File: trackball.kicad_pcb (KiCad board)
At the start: 2 copper layers, 27.5 x 35.2 mm, 37 parts, among them P1 CONN_10, P2 CONN_5, U1 MKL03Z32VFK4, U2 ADNS-3530, U4 ESD

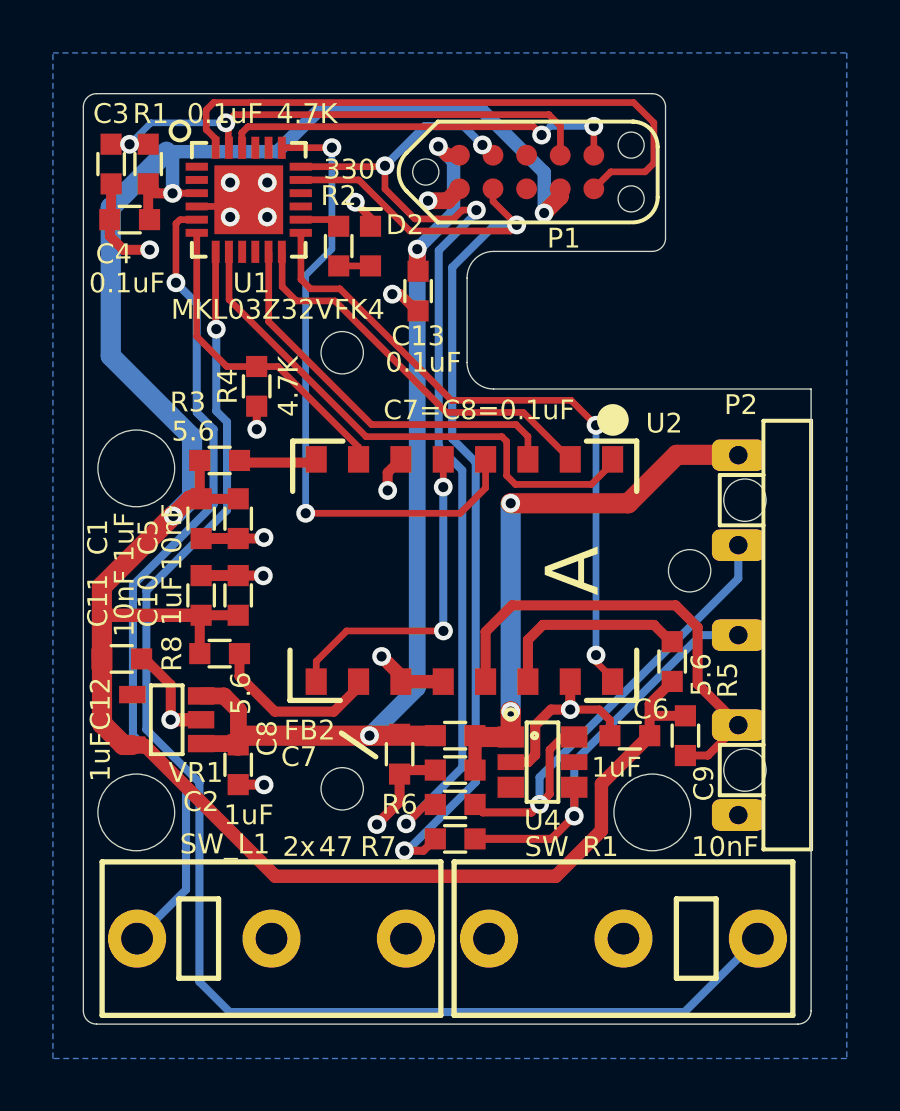
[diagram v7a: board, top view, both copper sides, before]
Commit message: Display optical sensor and microswitch part number on the silk screen.
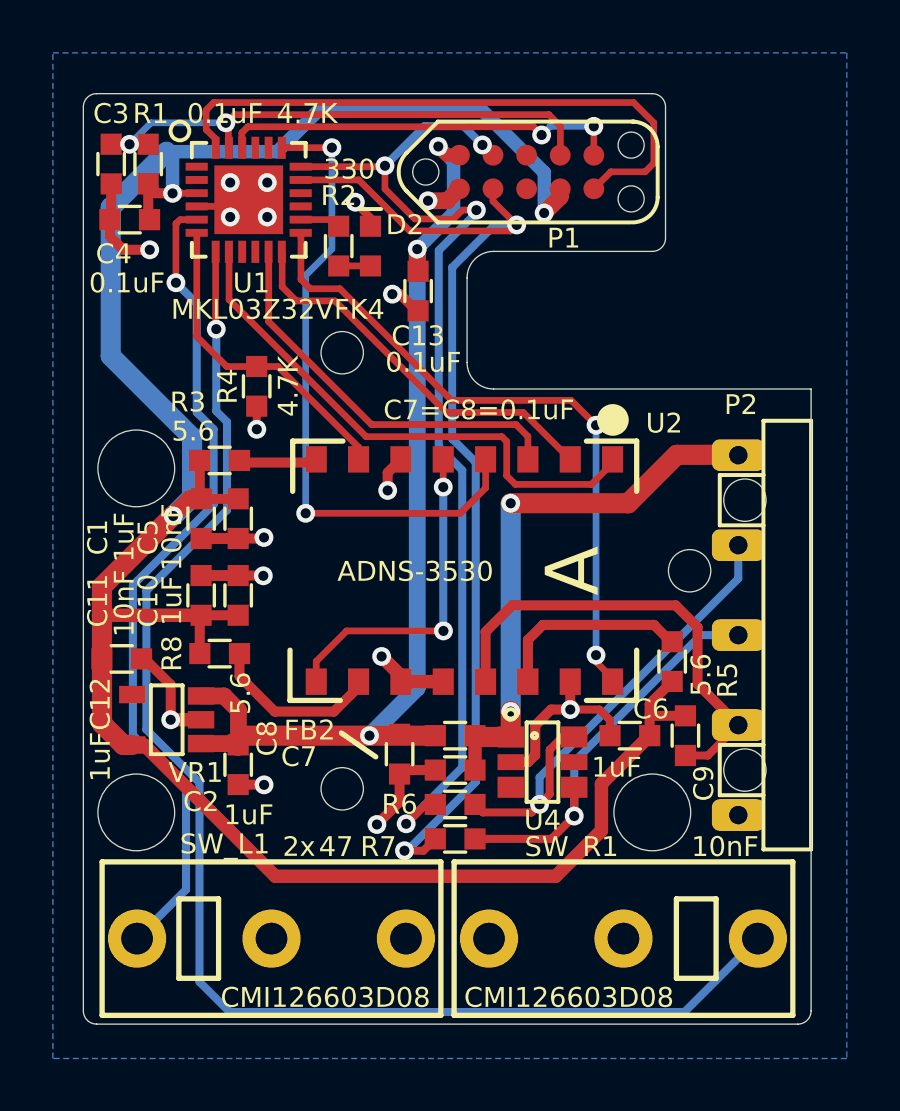
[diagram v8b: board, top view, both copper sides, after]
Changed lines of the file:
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@@
     (add_net "Net-(VR1-Pad4)")
+  )
+  (module ugl:CMI126603D08 locked (layer F.Cu)
+    (at 189.260001 144.468997)
+    (fp_text reference SW_L1 (at -1.760001 -3.568997) (layer F.SilkS)
+      (effects (font (size 0.75 0.75) (thickness 0.15)))
+    )
+    (fp_text value CMI126603D08 (at 2.039999 2.231003) (layer F.SilkS)
+      (effects (font (size 0.75 0.75) (thickness 0.15)))
+    )
+    (fp_line (start -3.5 1.5) (end -3.5 -1.5) (layer F.SilkS) (width 0.2))
+    (fp_line (start -2 1.5) (end -3.5 1.5) (layer F.SilkS) (width 0.2))
+    (fp_line (start -2 -1.5) (end -2 1.5) (layer F.SilkS) (width 0.2))
+    (fp_line (start -3.5 -1.5) (end -2 -1.5) (layer F.SilkS) (width 0.2))
+    (fp_line (start 6.4 -2.9) (end 6.4 2.9) (layer F.SilkS) (width 0.2))
+    (fp_line (start -6.4 2.9) (end 6.4 2.9) (layer F.SilkS) (width 0.2))
+    (fp_line (start -6.4 -2.9) (end -6.4 2.9) (layer F.SilkS) (width 0.2))
+    (fp_line (start 6.4 -2.9) (end -6.4 -2.9) (layer F.SilkS) (width 0.2))
+    (pad 3 thru_hole circle (at 5.08 0) (size 2.2 2.2) (drill 1.2) (layers *.Cu *.Mask))
+    (pad 2 thru_hole circle (at 0 0) (size 2.2 2.2) (drill 1.2) (layers *.Cu *.Mask)
+      (net 1 GND))
+    (pad 1 thru_hole circle (at -5.08 0) (size 2.2 2.2) (drill 1.2) (layers *.Cu *.Mask)
+      (net 5 /KEY_MLEFT))
   )
   (module ugl:ADNS-3530 locked (layer F.Cu)
@@
       (effects (font (size 0.746 0.746) (thickness 0.15)))
     )
-    (fp_text value ADNS-3530 (at -3.206242 7.484879) (layer F.Fab)
-      (effects (font (size 1 1) (thickness 0.15)))
+    (fp_text value ADNS-3530 (at -1.560001 0.030997) (layer F.SilkS)
+      (effects (font (size 0.75 0.75) (thickness 0.15)))
     )
     (fp_line (start -6.2 -4.9) (end -4.3 -4.9) (layer F.SilkS) (width 0.2))
@@
       (effects (font (size 0.75 0.75) (thickness 0.15)))
     )
-    (fp_text value CMI126603D08 (at 0 3.9) (layer F.Fab)
+    (fp_text value CMI126603D08 (at 2.060004 -2.231003) (layer F.SilkS)
       (effects (font (size 0.75 0.75) (thickness 0.15)))
     )
@@
       (net 6 /KEY_MRIGHT))
   )
-  (module ugl:CMI126603D08 locked (layer F.Cu)
-    (at 189.260001 144.468997)
-    (fp_text reference SW_L1 (at -1.760001 -3.568997) (layer F.SilkS)
-      (effects (font (size 0.75 0.75) (thickness 0.15)))
-    )
-    (fp_text value CMI126603D08 (at 0 3.9) (layer F.Fab)
-      (effects (font (size 0.75 0.75) (thickness 0.15)))
-    )
-    (fp_line (start -3.5 1.5) (end -3.5 -1.5) (layer F.SilkS) (width 0.2))
-    (fp_line (start -2 1.5) (end -3.5 1.5) (layer F.SilkS) (width 0.2))
-    (fp_line (start -2 -1.5) (end -2 1.5) (layer F.SilkS) (width 0.2))
-    (fp_line (start -3.5 -1.5) (end -2 -1.5) (layer F.SilkS) (width 0.2))
-    (fp_line (start 6.4 -2.9) (end 6.4 2.9) (layer F.SilkS) (width 0.2))
-    (fp_line (start -6.4 2.9) (end 6.4 2.9) (layer F.SilkS) (width 0.2))
-    (fp_line (start -6.4 -2.9) (end -6.4 2.9) (layer F.SilkS) (width 0.2))
-    (fp_line (start 6.4 -2.9) (end -6.4 -2.9) (layer F.SilkS) (width 0.2))
-    (pad 3 thru_hole circle (at 5.08 0) (size 2.2 2.2) (drill 1.2) (layers *.Cu *.Mask))
-    (pad 2 thru_hole circle (at 0 0) (size 2.2 2.2) (drill 1.2) (layers *.Cu *.Mask)
-      (net 1 GND))
-    (pad 1 thru_hole circle (at -5.08 0) (size 2.2 2.2) (drill 1.2) (layers *.Cu *.Mask)
-      (net 5 /KEY_MLEFT))
-  )
   (module ugl:Tag_Connect_2x5_Header_With_No_Legs_Parallel_Numbering (layer F.Cu)
